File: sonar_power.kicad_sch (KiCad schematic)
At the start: 0 parts

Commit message: Created hierarchical sheets and porting some stuff in from Lumen
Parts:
- added C7: 100nF 25V, BR_Passives:C_0201_0603Metric-minimized, symbol BR_Capacitors_0201:C_0201_100nF_25V_X7R_10%
- added R15: 47k, BR_Passives:R_0201_0603Metric-minimized, symbol BR_Resistors_0201:R_0201_47k
- added R18: 3k, BR_Passives:R_0201_0603Metric-minimized, symbol BR_Resistors_0201:R_0201_3k
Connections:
- new net GND: C7.2, R18.2
- new net VIN_PROTECTED: R15.1
- new net V_SENSE: C7.1, R15.2, R18.1
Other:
- added sheet 3V3 Buck (lumen2_3v3_buck.kicad_sch)

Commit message: power sheets
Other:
- added sheet 1V8 Buck (1v8_buck.kicad_sch)
- added sheet 48V Boost (48v_boost.kicad_sch)
- added sheet 4V5 Buck (4v5_buck.kicad_sch)
- added sheet 5V Buck (5v_buck.kicad_sch)
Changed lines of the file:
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@@
-	)
-	(junction
-		(at 66.04 69.85)
-		(diameter 0)
-		(color 0 0 0 0)
 	)
 	(junction
@@
 	(wire
 		(pts
-			(xy 133.35 69.85) (xy 104.14 69.85)
+			(xy 190.5 133.35) (xy 161.29 133.35)
 		)
 		(stroke
@@
 		(pts
 			(xy 83.82 100.33) (xy 88.9 100.33)
-		)
-		(stroke
-			(width 0)
-			(type default)
-		)
-	)
-	(wire
-		(pts
-			(xy 66.04 69.85) (xy 81.28 69.85)
 		)
 		(stroke
@@
 	(hierarchical_label "3V3"
 		(shape input)
-		(at 133.35 69.85 0)
+		(at 190.5 133.35 0)
 		(effects
 			(font
@@
 	)
 	(sheet
-		(at 81.28 64.77)
+		(at 127 38.1)
+		(size 25.4 25.4)
+		(exclude_from_sim no)
+		(in_bom yes)
+		(on_board yes)
+		(dnp no)
+		(fields_autoplaced yes)
+		(stroke
+			(width 0.1524)
+			(type solid)
+		)
+		(fill
+			(color 0 0 0 0.0000)
+		)
+		(property "Sheetname" "3V3 Buck"
+			(at 127 37.3884 0)
+			(effects
+				(font
+					(size 1.27 1.27)
+				)
+				(justify left bottom)
+			)
+		)
+		(property "Sheetfile" "3v3_buck.kicad_sch"
+			(at 127 64.0846 0)
+			(effects
+				(font
+					(size 1.27 1.27)
+				)
+				(justify left top)
+			)
+		)
+		(instances
+			(project "SonarDevBoard"
+				(path "/2a5ce3ef-537a-4122-a1be-ef76186bc0d7/774f2c6c-c15c-4713-acf0-4edb2ec6be20"
+					(page "12")
+				)
+			)
+		)
+	)
+	(sheet
+		(at 165.1 38.1)
+		(size 25.4 25.4)
+		(exclude_from_sim no)
+		(in_bom yes)
+		(on_board yes)
+		(dnp no)
+		(fields_autoplaced yes)
+		(stroke
+			(width 0.1524)
+			(type solid)
+		)
+		(fill
+			(color 0 0 0 0.0000)
+		)
+		(property "Sheetname" "1V8 Buck"
+			(at 165.1 37.3884 0)
+			(effects
+				(font
+					(size 1.27 1.27)
+				)
+				(justify left bottom)
+			)
+		)
+		(property "Sheetfile" "1v8_buck.kicad_sch"
+			(at 165.1 64.0846 0)
+			(effects
+				(font
+					(size 1.27 1.27)
+				)
+				(justify left top)
+			)
+		)
+		(instances
+			(project "SonarDevBoard"
+				(path "/2a5ce3ef-537a-4122-a1be-ef76186bc0d7/774f2c6c-c15c-4713-acf0-4edb2ec6be20"
+					(page "13")
+				)
+			)
+		)
+	)
+	(sheet
+		(at 88.9 38.1)
+		(size 25.4 25.4)
+		(exclude_from_sim no)
+		(in_bom yes)
+		(on_board yes)
+		(dnp no)
+		(fields_autoplaced yes)
+		(stroke
+			(width 0.1524)
+			(type solid)
+		)
+		(fill
+			(color 0 0 0 0.0000)
+		)
+		(property "Sheetname" "4V5 Buck"
+			(at 88.9 37.3884 0)
+			(effects
+				(font
+					(size 1.27 1.27)
+				)
+				(justify left bottom)
+			)
+		)
+		(property "Sheetfile" "4v5_buck.kicad_sch"
+			(at 88.9 64.0846 0)
+			(effects
+				(font
+					(size 1.27 1.27)
+				)
+				(justify left top)
+			)
+		)
+		(instances
+			(project "SonarDevBoard"
+				(path "/2a5ce3ef-537a-4122-a1be-ef76186bc0d7/774f2c6c-c15c-4713-acf0-4edb2ec6be20"
+					(page "11")
+				)
+			)
+		)
+	)
+	(sheet
+		(at 138.43 128.27)
 		(size 22.86 22.86)
 		(exclude_from_sim no)
@@
 		)
 		(property "Sheetname" "3V3 Buck"
-			(at 81.28 64.0584 0)
+			(at 138.43 127.5584 0)
 			(effects
 				(font
@@
 		)
 		(property "Sheetfile" "lumen2_3v3_buck.kicad_sch"
-			(at 81.28 88.2146 0)
+			(at 138.43 151.7146 0)
 			(effects
 				(font
@@
 		)
 		(pin "VIN" input
-			(at 81.28 69.85 180)
+			(at 138.43 133.35 180)
 			(effects
 				(font
@@
 		)
 		(pin "3V3" input
-			(at 104.14 69.85 0)
+			(at 161.29 133.35 0)
 			(effects
 				(font
@@
 				)
 			)
+		)
+	)
+	(sheet
+		(at 241.3 38.1)
+		(size 25.4 26.67)
+		(exclude_from_sim no)
+		(in_bom yes)
+		(on_board yes)
+		(dnp no)
+		(fields_autoplaced yes)
+		(stroke
+			(width 0.1524)
+			(type solid)
+		)
+		(fill
+			(color 0 0 0 0.0000)
+		)
+		(property "Sheetname" "5V Buck"
+			(at 241.3 37.3884 0)
+			(effects
+				(font
+					(size 1.27 1.27)
+				)
+				(justify left bottom)
+			)
+		)
+		(property "Sheetfile" "5v_buck.kicad_sch"
+			(at 241.3 65.3546 0)
+			(effects
+				(font
+					(size 1.27 1.27)
+				)
+				(justify left top)
+			)
+		)
+		(instances
+			(project "SonarDevBoard"
+				(path "/2a5ce3ef-537a-4122-a1be-ef76186bc0d7/774f2c6c-c15c-4713-acf0-4edb2ec6be20"
+					(page "15")
+				)
+			)
+		)
+	)
+	(sheet
+		(at 203.2 38.1)
+		(size 25.4 25.4)
+		(exclude_from_sim no)
+		(in_bom yes)
+		(on_board yes)
+		(dnp no)
+		(fields_autoplaced yes)
+		(stroke
+			(width 0.1524)
+			(type solid)
+		)
+		(fill
+			(color 0 0 0 0.0000)
+		)
+		(property "Sheetname" "48V Boost"
+			(at 203.2 37.3884 0)
+			(effects
+				(font
+					(size 1.27 1.27)
+				)
+				(justify left bottom)
+			)
+		)
+		(property "Sheetfile" "48v_boost.kicad_sch"
+			(at 203.2 64.0846 0)
+			(effects
+				(font
+					(size 1.27 1.27)
+				)
+				(justify left top)
+			)
+		)
+		(instances
+			(project "SonarDevBoard"
+				(path "/2a5ce3ef-537a-4122-a1be-ef76186bc0d7/774f2c6c-c15c-4713-acf0-4edb2ec6be20"
+					(page "14")
+				)
+			)

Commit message: power scheme
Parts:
- added R104: 45k3, BR_Passives:R_0201_0603Metric-minimized, symbol BR_Resistors_0201:R_0201_45k3
- added R112: 20k, BR_Passives:R_0201_0603Metric-minimized, symbol BR_Resistors_0201:R_0201_20k
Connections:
- net 3V3: now also R104.1
- net VIN_PROTECTED: now also R15.2; no longer R15.1
- net V_SENSE: now also R15.1; no longer R15.2
- new net 1V8: R112.1
- new net 1V8 Buck/RSET: R112.2
- new net 3V3 Buck/RSET: R104.2
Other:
- sheet 1V8 Buck ports: added EN, RSET, VIN, VOUT; removed none
- sheet 3V3 Buck: file lumen2_3v3_buck.kicad_sch -> 3v3_buck.kicad_sch
- sheet 3V3 Buck ports: added EN, RSET, VOUT; removed 3V3
- moved on the sheet: C7, R15, R18

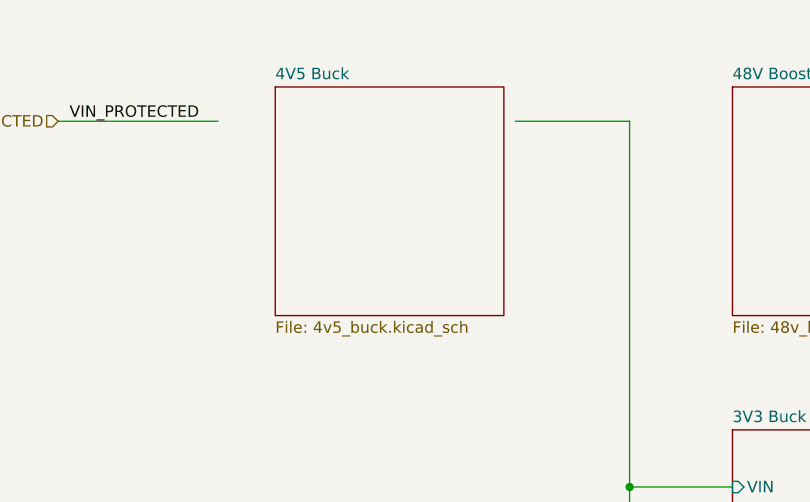
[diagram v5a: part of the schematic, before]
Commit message: edits to 4V buck
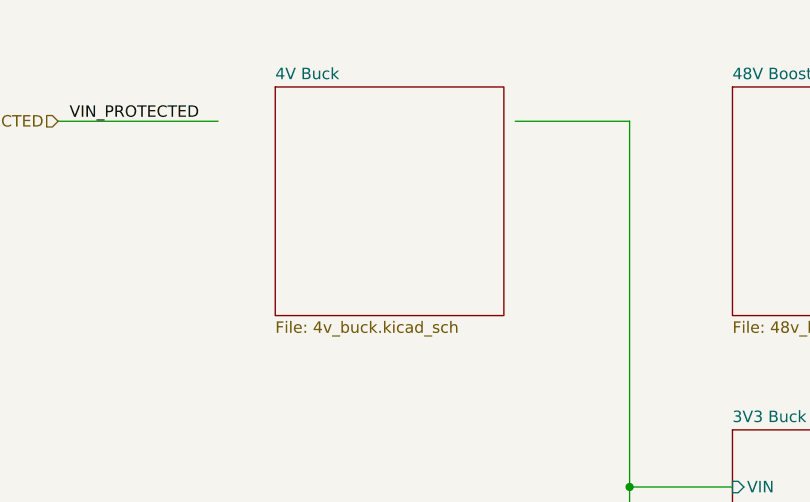
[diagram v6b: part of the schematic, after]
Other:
- sheet 4V5 Buck renamed 4V Buck
- sheet 4V Buck: file 4v5_buck.kicad_sch -> 4v_buck.kicad_sch
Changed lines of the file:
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@@
 			(color 0 0 0 0.0000)
 		)
-		(property "Sheetname" "4V5 Buck"
+		(property "Sheetname" "4V Buck"
 			(at 76.2 37.3884 0)
 			(effects
@@
 			)
 		)
-		(property "Sheetfile" "4v5_buck.kicad_sch"
+		(property "Sheetfile" "4v_buck.kicad_sch"
 			(at 76.2 64.0846 0)
 			(effects

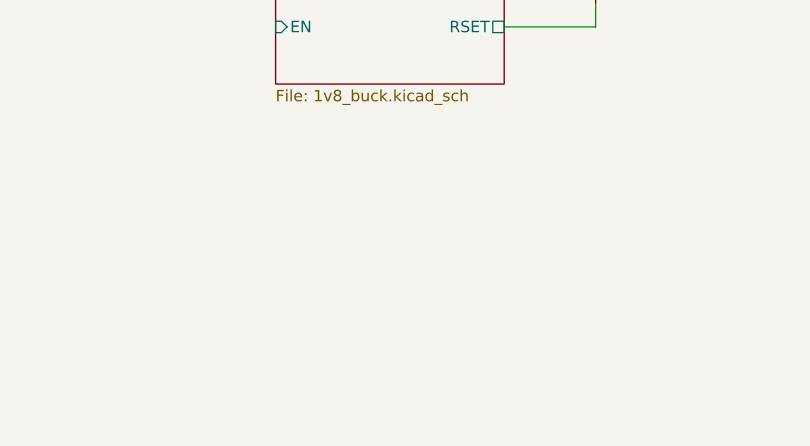
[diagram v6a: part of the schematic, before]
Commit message: Added 7V boost subsheet
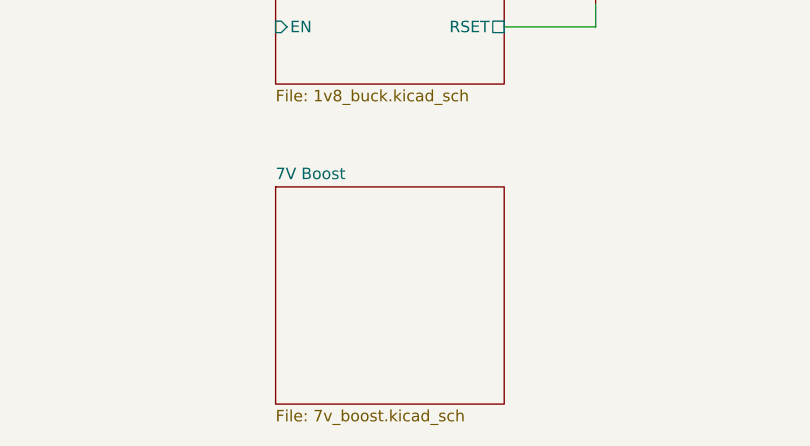
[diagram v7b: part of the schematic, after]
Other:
- added sheet 7V Boost (7v_boost.kicad_sch)
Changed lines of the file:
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@@
+	)
+	(sheet
+		(at 127 151.13)
+		(size 25.4 24.13)
+		(exclude_from_sim no)
+		(in_bom yes)
+		(on_board yes)
+		(dnp no)
+		(fields_autoplaced yes)
+		(stroke
+			(width 0.1524)
+			(type solid)
+		)
+		(fill
+			(color 0 0 0 0.0000)
+		)
+		(property "Sheetname" "7V Boost"
+			(at 127 150.4184 0)
+			(effects
+				(font
+					(size 1.27 1.27)
+				)
+				(justify left bottom)
+			)
+		)
+		(property "Sheetfile" "7v_boost.kicad_sch"
+			(at 127 175.8446 0)
+			(effects
+				(font
+					(size 1.27 1.27)
+				)
+				(justify left top)
+			)
+		)
+		(instances
+			(project "SonarDevBoard"
+				(path "/2a5ce3ef-537a-4122-a1be-ef76186bc0d7/774f2c6c-c15c-4713-acf0-4edb2ec6be20"
+					(page "15")
+				)
+			)
+		)
 	)
 	(sheet

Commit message: power scheme updates
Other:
- sheet 5V Buck renamed 5V LDO
- sheet 4V Buck ports: added VIN, VOUT; removed none
- sheet 5V LDO: file 5v_buck.kicad_sch -> 5v_ldo.kicad_sch
- moved on the sheet: C7, R104, R112, R15, R18
